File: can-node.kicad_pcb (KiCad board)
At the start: 2 copper layers, 50 x 60 mm, 109 parts, among them P1 Debug, P2 CONN_01X04, Q1 DMP6023LSS, Q10 BSS138, Q11 BSS84P, Q12 BSS84P, Q13 BSS84P, Q14 BSS84P, Q15 BSS84P, Q2 SFH3711, Q3 BSS138, Q4 BSS138, Q5 BSS138, Q6 BSS138, Q7 BSS138, Q8 BSS138, Q9 BSS138, SW1 SW_PUSH, SW2 SW_PUSH, SW3 SW_PUSH, U1 LMR16006, U2 SN74LVC1G08, U3 STM32F072RB, U4 HDC1080, U5 TCAN334, X1 32.768KHz 12.5pF

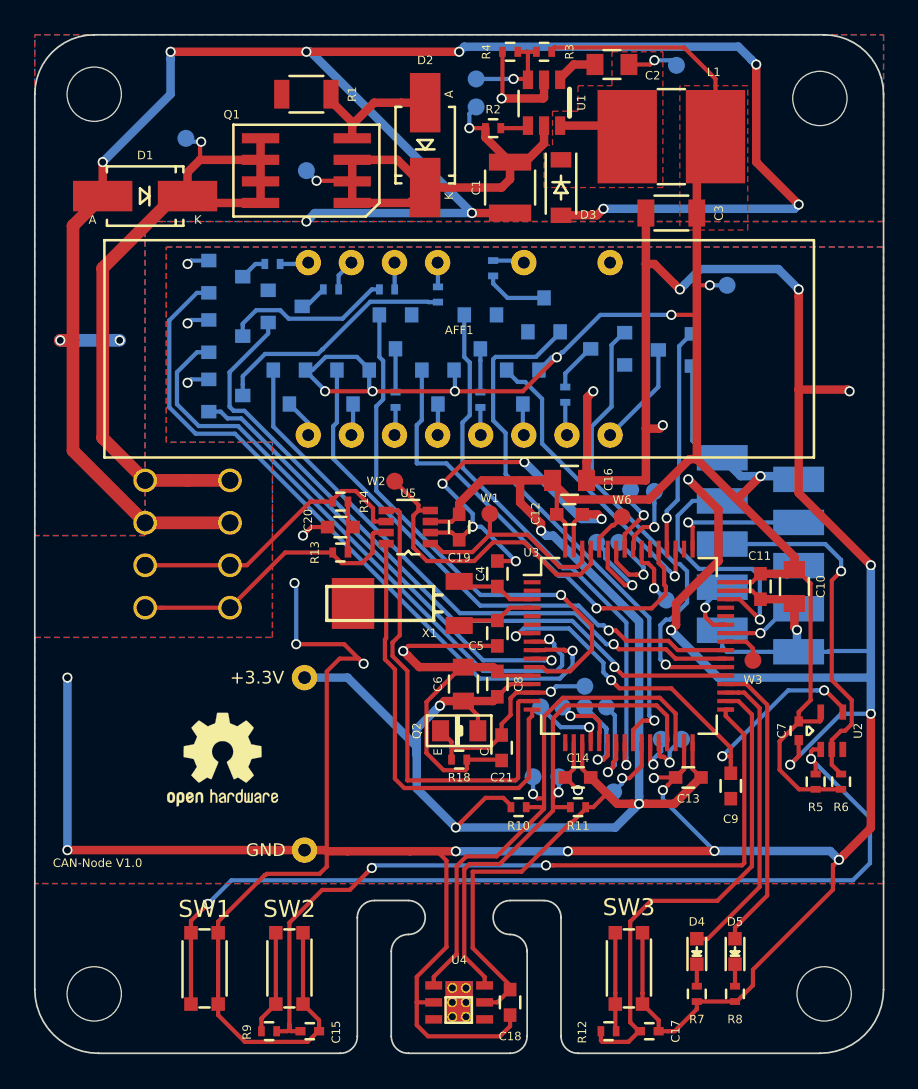
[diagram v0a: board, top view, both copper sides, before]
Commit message: Add buffer capacitor for RTC.
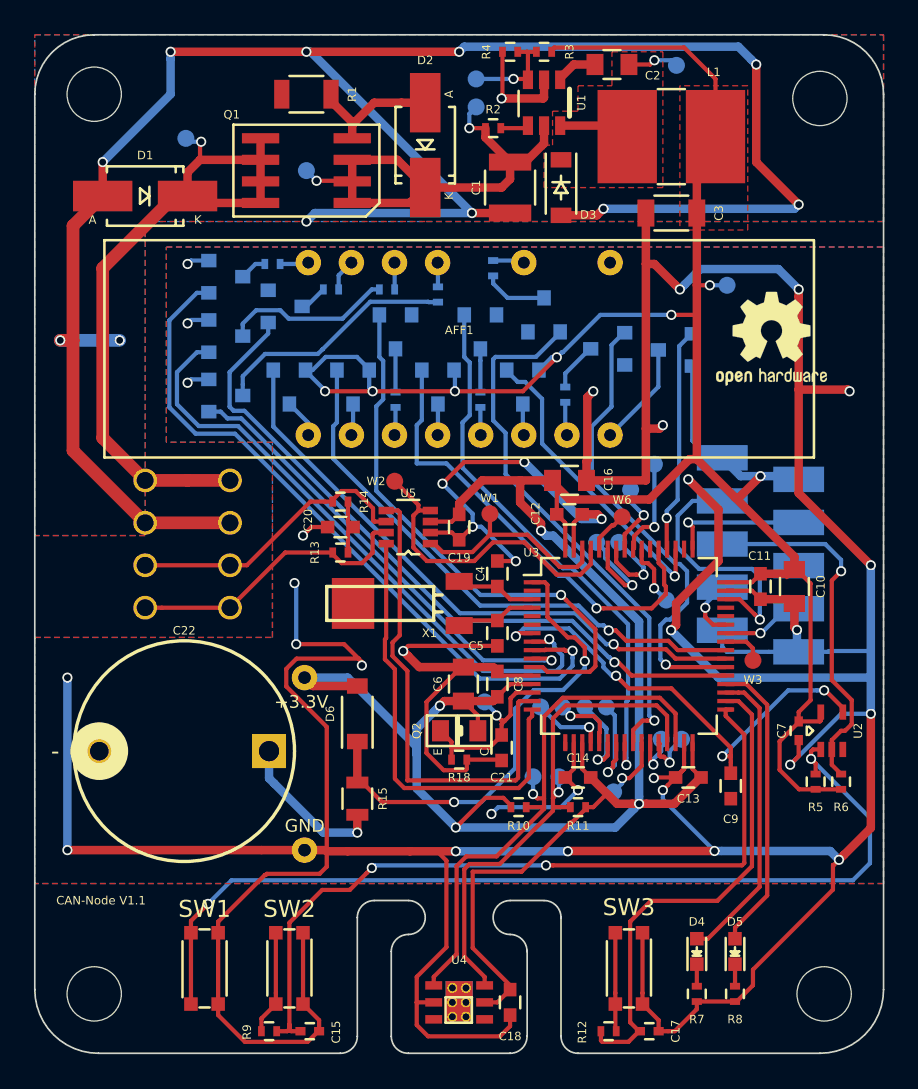
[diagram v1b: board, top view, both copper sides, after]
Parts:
- added C22: 0.1F, can-node:C_Radial_D13_L7_P10, F.Cu at (133.8, 107.2)
- added D6: 0.3V, Diodes_SMD:SOD-123, F.Cu at (139.0, 105.0)
- added R15: 100, Resistors_SMD:R_0805, F.Cu at (139.0, 110.0)
- R12, R9: value 220 -> 3.3k
- moved REF*** 40.7 mm to (163.4, 82.9)
- moved W18 5.97 mm to (146.5, 104.3)
- moved W35 1.60 mm to (156.5, 90.3)
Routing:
- net VBAT: track 0.00 -> 28.6 mm, vias 0 -> 2
- net GND: track 472.2 -> 481.4 mm, vias 45 -> 46
- net Net-(C22-Pad1): track 0.00 -> 9.18 mm, vias 0 -> 1
- net +3.3VADC: track 236.3 -> 239.7 mm
- net /Microcontroller/PB4: track 4.30 -> 5.90 mm
- net /Microcontroller/ADC_IN0: track 12.3 -> 10.8 mm
- net PC3: track 32.2 -> 33.1 mm
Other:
- board text added: "CAN-Node V1.1"
- board text removed: "CAN-Node V1.0"

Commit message: Make the board more hand solder friendly.
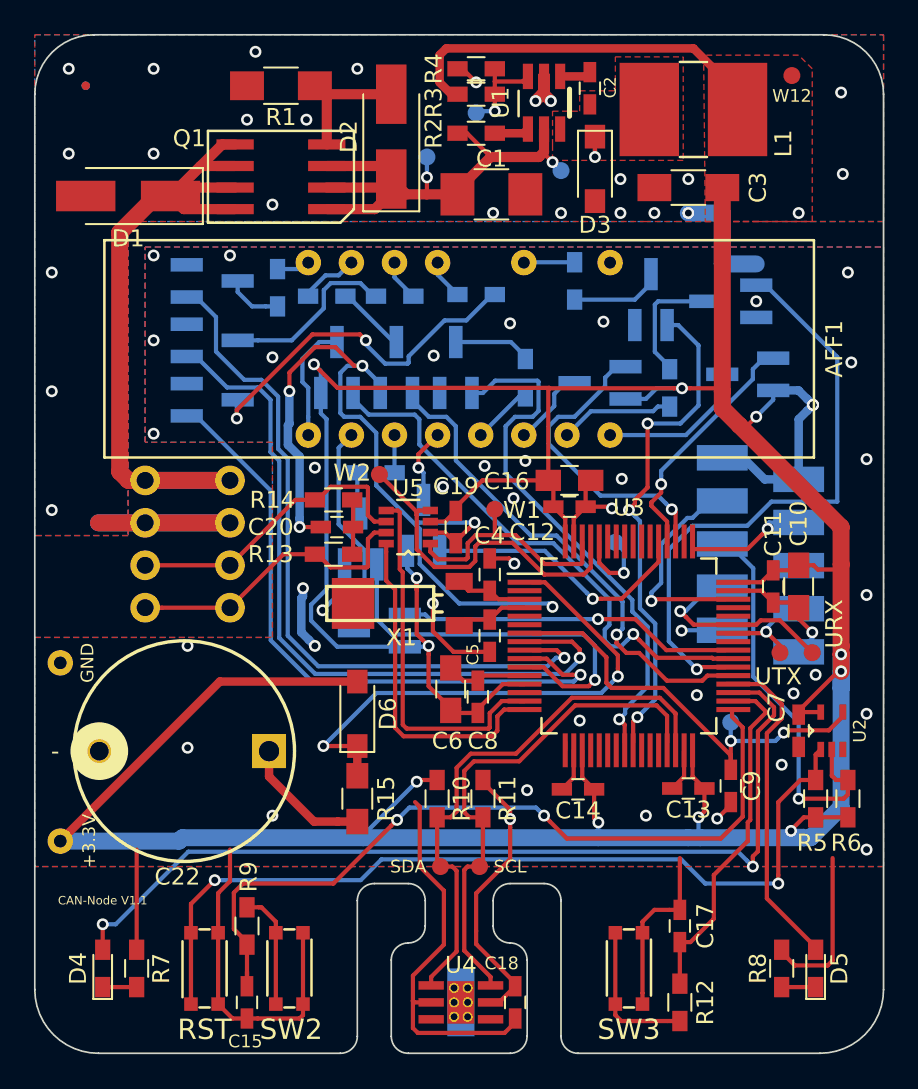
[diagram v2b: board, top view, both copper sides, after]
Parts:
- removed C21: 100n, Capacitors_SMD:C_0603
- removed Q2: SFH3711, can-node:SFH3711
- removed R18: 4.7k, Resistors_SMD:R_0402
- removed the REF** at (166.5, 121.5)
- removed the REF** at (166.2, 68.8)
- removed the REF** at (123.5, 68.5)
- removed the REF** at (123.5, 121.5)
- removed the REF*** at (163.4, 82.9)
- removed W13: PA5, can-node:Measurement_Point_tiny
- removed W14: PA4, can-node:Measurement_Point_tiny
- removed W18: LSENS, can-node:Measurement_Point_tiny
- removed W30: PB2, can-node:Measurement_Point_tiny
- removed W31: PB1, can-node:Measurement_Point_tiny
- removed W32: PB0, can-node:Measurement_Point_tiny
- removed W33, W34, W35, W36, W37: PB, can-node:Measurement_Point_tiny
- removed W4: PA7, can-node:Measurement_Point_tiny
- removed W5: PA6, can-node:Measurement_Point_tiny
- removed W7: VINA, can-node:Measurement_Point_tiny
- added REF**: Fiducial_0.5mm_Dia_1mm_Outer, Fiducials:Fiducial_0.5mm_Dia_1mm_Outer, F.Cu at (123.0, 68.0)
- added REF**: Fiducial_0.5mm_Dia_1mm_Outer, Fiducials:Fiducial_0.5mm_Dia_1mm_Outer, B.Cu at (123.0, 68.0)
- added REF***: OSHW-Logo_7.5x8mm_SilkScreen, Symbols:OSHW-Logo_7.5x8mm_SilkScreen, B.Cu at (160.5, 118.2)
- added URX: UART_RX, can-node:Measurement_Point_tiny, F.Cu at (165.8, 101.4)
- added UTX: UART_TX, can-node:Measurement_Point_tiny, F.Cu at (163.9, 101.4)
- C1: footprint Capacitors_SMD:C_1210 -> Capacitors_SMD:C_1210_HandSoldering
- C10, C16, C6: footprint Capacitors_SMD:C_0805 -> Capacitors_SMD:C_0805_HandSoldering
- C11, C12, C13, C14, C18, C19, C20, C4, C5, C8, C9: footprint Capacitors_SMD:C_0603 -> Capacitors_SMD:C_0603_HandSoldering
- C15, C17, C7: footprint Capacitors_SMD:C_0402 -> Capacitors_SMD:C_0603_HandSoldering
- C2: footprint Capacitors_SMD:C_0805 -> Capacitors_SMD:C_0603_HandSoldering
- C3: footprint Capacitors_SMD:C_1206 -> Capacitors_SMD:C_1206_HandSoldering
- D1, D2: footprint Diodes_SMD:SMA_Handsoldering -> Diodes_SMD:D_SMA_Handsoldering
- D3, D6: footprint Diodes_SMD:SOD-123 -> can-node:D_SOD-123_HandSoldering
- D4, D5: footprint LEDs:LED_0603 -> LEDs:LED_0603_HandSoldering
- L1: footprint CAN_Node:SDE0604A_HandSoldering -> can-node:SDE0604A_HandSoldering
- P1: footprint CAN_Node:micromatch_smd_2x05 -> can-node:micromatch_smd_2x05
- Q10, Q11, Q12, Q13, Q14, Q15, Q3, Q4, Q5, Q6, Q7, Q8, Q9: footprint TO_SOT_Packages_SMD:SOT-23 -> TO_SOT_Packages_SMD:SOT-23_Handsoldering
- R1: footprint Resistors_SMD:R_1206 -> Resistors_SMD:R_1206_HandSoldering
- R10, R11, R12, R13, R14, R2, R25, R26, R27, R28, R3, R33, R34, R35, R36, R4, R5, R6, R7, R8, R9: footprint Resistors_SMD:R_0402 -> Resistors_SMD:R_0603_HandSoldering
- R15: footprint Resistors_SMD:R_0805 -> Resistors_SMD:R_0805_HandSoldering
- SCL: renamed from W17; moved to F.Cu
- SDA: renamed from W16; moved to F.Cu
- SW2, SW3: footprint CAN_Node:KMR2 -> can-node:KMR2
- U1: footprint can-node:TI-DDC -> can-node:TI-DDC_HandSoldering
- U2: footprint CAN_Node:TI-DCK -> can-node:TI-DCK
- U3: footprint Housings_QFP:LQFP-64_10x10mm_Pitch0.5mm -> can-node:QFP-64_10x10_Pitch0.5mm_HandSoldering
- U4: footprint CAN_Node:HDC1080 -> can-node:HDC1080_HandSoldering
- U5: footprint CAN_Node:TI-DCN -> can-node:TI-DCN
- W12: moved to F.Cu
- W15: value TEST_1P -> 3.3V
- W19: value TEST_1P -> GND
- W3: value PA8 -> ~RST; moved to B.Cu
- W6: moved to B.Cu
- moved D4 35.0 mm to (124.0, 120.0)
- moved R7 33.0 mm to (126.0, 120.0), turned to 270 degrees
- moved W19 18.1 mm to (121.5, 102.0)
- moved W15 17.3 mm to (121.5, 112.5)
- moved Q12 14.4 mm to (140.3, 100.1), turned to 180 degrees
- moved W12 12.9 mm to (164.6, 67.4)
- moved Q6 12.4 mm to (139.2, 94.7), turned to 90 degrees
- moved Q15 8.19 mm to (142.9, 93.9), turned to 90 degrees
- moved Q10 7.77 mm to (161.0, 80.7)
- moved SDA 7.60 mm to (143.9, 114.0)
- moved Q9 7.47 mm to (141.3, 84.6), turned to 90 degrees
- moved W8 7.14 mm to (143.1, 72.2), turned to 0 degrees
- moved SCL 7.06 mm to (146.2, 114.0)
- moved C17 6.46 mm to (158.0, 117.5), turned to 90 degrees
- moved W11 6.38 mm to (153.0, 71.0), turned to 0 degrees
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- renumbered SW1 to RST
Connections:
- U3 pad 14: /Microcontroller/ADC_IN0 -> Net-(U3-Pad14)
- U3 pad 26: /Microcontroller/PB0 -> Net-(U3-Pad26)
- U3 pad 27: /Microcontroller/PB1 -> Net-(U3-Pad27)
- U3 pad 28: /Microcontroller/PB2 -> Net-(U3-Pad28)
- U3 pad 55: /Microcontroller/PB3 -> Net-(U3-Pad55)
- U3 pad 56: /Microcontroller/PB4 -> Net-(U3-Pad56)
- U3 pad 57: /Microcontroller/PB5 -> Net-(U3-Pad57)
- U3 pad 58: /Microcontroller/PB6 -> Net-(U3-Pad58)
- U3 pad 59: /Microcontroller/PB7 -> Net-(U3-Pad59)
- W3 pad 1: Net-(U3-Pad41) -> Net-(C9-Pad1)
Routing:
- net GND: track 481.4 -> 185.2 mm, vias 46 -> 69
- net +3.3VADC: track 239.7 -> 287.4 mm, vias 11 -> 15
- net Net-(D4-Pad2): track 17.9 -> 55.0 mm, vias 0 -> 2
- net PC9: track 33.1 -> 19.8 mm
- net PC6: track 41.7 -> 29.0 mm
- net PC12: track 27.1 -> 15.7 mm
- net Net-(AFF1-Pad2): track 1.87 -> 12.7 mm
- net PC2: track 27.4 -> 38.3 mm
- net /Microcontroller/ADC_IN0: track 10.8 -> 0.00 mm, vias 1 -> 0
- net PC3: track 33.1 -> 23.1 mm
- net PC7: track 27.4 -> 35.6 mm
- net /Microcontroller/UART1_RX: track 3.56 -> 11.6 mm
- net Net-(C17-Pad1): track 29.2 -> 21.1 mm
- net Net-(U3-Pad22): track 7.25 -> 0.00 mm, vias 1 -> 0
- net Net-(Q5-Pad3): track 14.5 -> 21.4 mm, vias 0 -> 2
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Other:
- outline, holes or cut-outs redrawn
- net class Default: via_dia 0.6 -> 0.7
- net class Power: via_dia 0.6 -> 0.7
- rule via_min_drill: 0.3 -> 0.4
- rule via_min_size: 0.4 -> 0.7
- board text added: "+"
- board text added: "-"
- board text added: "2018-01-05"
- board text added: "CAN Node Rev 1.1"
- board text added: "CH"
- board text added: "CL"
- board text added: "designed with KiCad"
- board text removed: "3.3V"
- board text removed: "CANH"
- board text removed: "CANL"
- board text removed: "SWCLK"
- board text removed: "SWDIO"
- board text removed: "U_TX"
- board text removed: "VIN+/24V DC"
- board text removed: "VIN-/0V"
- board text removed: "designed with KiCAD"
- board text removed: "© 2017 Josef Raschen"

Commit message: Add mounting holes.
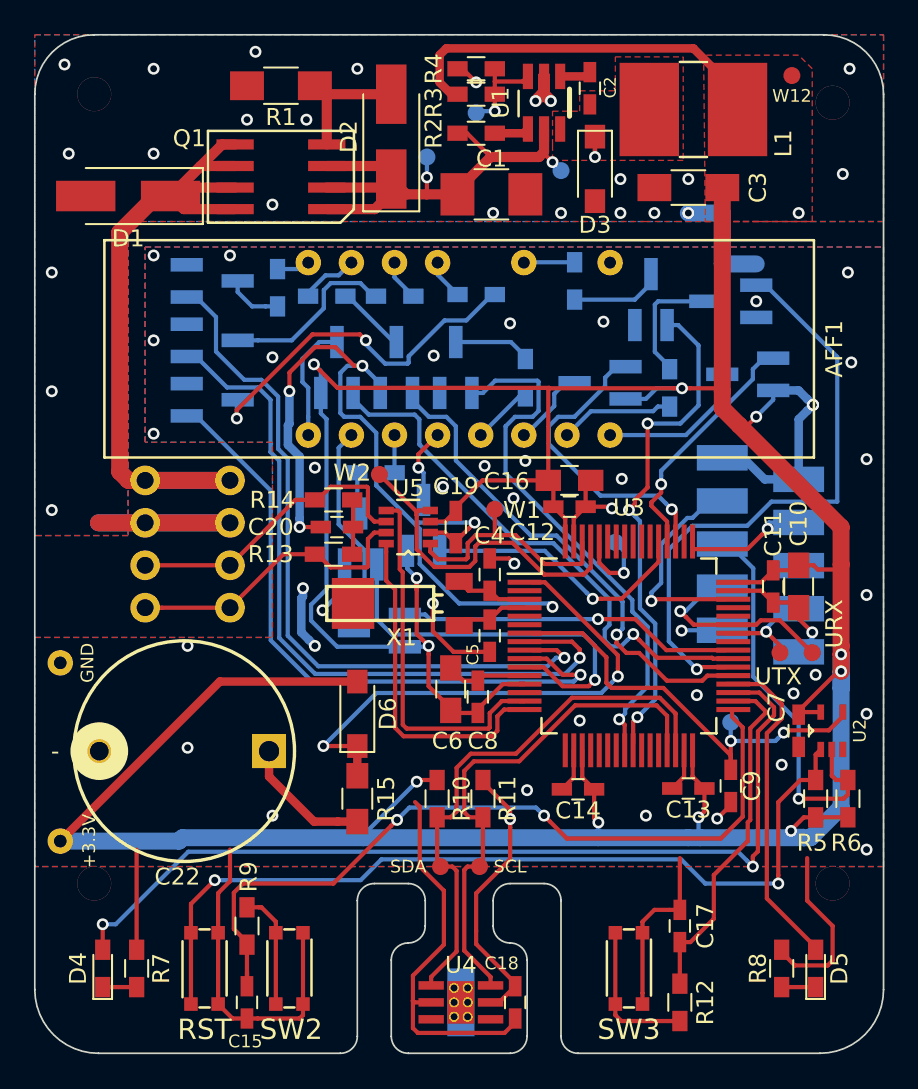
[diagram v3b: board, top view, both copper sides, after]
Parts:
- removed the REF** at (123.0, 68.0) (x2)
- added REF**: NPTH_2mm, can-node:NPTH_2mm, F.Cu at (167.0, 115.0)
- added REF**: NPTH_2mm, can-node:NPTH_2mm, F.Cu at (123.5, 115.0)
- added REF**: NPTH_2mm, can-node:NPTH_2mm, F.Cu at (167.0, 69.0)
- added REF**: NPTH_2mm, can-node:NPTH_2mm, F.Cu at (123.5, 68.5)
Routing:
- net GND: track 185.2 -> 185.8 mm
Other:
- board text removed: "CAN-Node V1.1"
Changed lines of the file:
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@@
   (general
     (thickness 1.6)
-    (drawings 75)
-    (tracks 993)
+    (drawings 74)
+    (tracks 995)
     (zones 0)
-    (modules 95)
+    (modules 97)
     (nets 98)
   )
@@
   )
   (setup
-    (last_trace_width 1)
+    (last_trace_width 0.25)
     (user_trace_width 0.2)
     (user_trace_width 0.5)
@@
     (mod_text_size 1 1)
     (mod_text_width 0.2)
-    (pad_size 1.5 1.5)
-    (pad_drill 0.6)
+    (pad_size 2 2)
+    (pad_drill 2)
     (pad_to_mask_clearance 0)
     (aux_axis_origin 0 0)
@@
     (add_net VIN+)
   )
+  (module can-node:NPTH_2mm (layer F.Cu)
+    (at 167 115)
+    (fp_text reference REF** (at 0 0.5) (layer F.SilkS) hide
+      (effects (font (size 1 1) (thickness 0.15)))
+    )
+    (fp_text value NPTH_2mm (at 0 -0.5) (layer F.Fab) hide
+      (effects (font (size 1 1) (thickness 0.15)))
+    )
+    (pad "" thru_hole circle (at 0 0) (size 2 2) (drill 2) (layers *.Cu *.Mask))
+  )
+  (module can-node:NPTH_2mm (layer F.Cu)
+    (at 123.5 115)
+    (fp_text reference REF** (at 0 0.5) (layer F.SilkS) hide
+      (effects (font (size 1 1) (thickness 0.15)))
+    )
+    (fp_text value NPTH_2mm (at 0 -0.5) (layer F.Fab) hide
+      (effects (font (size 1 1) (thickness 0.15)))
+    )
+    (pad "" thru_hole circle (at 0 0) (size 2 2) (drill 2) (layers *.Cu *.Mask))
+  )
+  (module can-node:NPTH_2mm (layer F.Cu)
+    (at 167 69)
+    (fp_text reference REF** (at 0 0.5) (layer F.SilkS) hide
+      (effects (font (size 1 1) (thickness 0.15)))
+    )
+    (fp_text value NPTH_2mm (at 0 -0.5) (layer F.Fab) hide
+      (effects (font (size 1 1) (thickness 0.15)))
+    )
+    (pad "" thru_hole circle (at 0 0) (size 2 2) (drill 2) (layers *.Cu *.Mask))
+  )
+  (module can-node:NPTH_2mm (layer F.Cu)
+    (at 123.5 68.5)
+    (fp_text reference REF** (at 0 0.5) (layer F.SilkS) hide
+      (effects (font (size 1 1) (thickness 0.15)))
+    )
+    (fp_text value NPTH_2mm (at 0 -0.5) (layer F.Fab) hide
+      (effects (font (size 1 1) (thickness 0.15)))
+    )
+    (pad "" thru_hole circle (at 0 0) (size 2 2) (drill 2) (layers *.Cu *.Mask))
+  )
   (module can-node:HDC1080_HandSoldering (layer F.Cu)
     (at 145.1 122 270)
@@
       (net 5 +3.3VADC))
   )
-  (module Fiducials:Fiducial_0.5mm_Dia_1mm_Outer (layer F.Cu)
-    (at 123 68)
-    (descr "Circular Fiducial, 0.5mm bare copper top; 1mm keepout (Level C)")
-    (tags marker)
-    (attr virtual)
-    (fp_text reference REF** (at 0 -1.5) (layer F.SilkS) hide
-      (effects (font (size 1 1) (thickness 0.15)))
-    )
-    (fp_text value Fiducial_0.5mm_Dia_1mm_Outer (at 0 1.5) (layer F.Fab)
-      (effects (font (size 1 1) (thickness 0.15)))
-    )
-    (fp_circle (center 0 0) (end 0.5 0) (layer F.Fab) (width 0.1))
-    (fp_text user %R (at 0 0) (layer F.Fab)
-      (effects (font (size 0.2 0.2) (thickness 0.04)))
-    )
-    (fp_circle (center 0 0) (end 0.75 0) (layer F.CrtYd) (width 0.05))
-    (pad ~ smd circle (at 0 0) (size 0.5 0.5) (layers F.Cu F.Mask)
-      (solder_mask_margin 0.25) (clearance 0.25))
-  )
-  (module Fiducials:Fiducial_0.5mm_Dia_1mm_Outer (layer B.Cu)
-    (at 123 68)
-    (descr "Circular Fiducial, 0.5mm bare copper top; 1mm keepout (Level C)")
-    (tags marker)
-    (attr virtual)
-    (fp_text reference REF** (at 0 1.5) (layer B.SilkS) hide
-      (effects (font (size 1 1) (thickness 0.15)) (justify mirror))
-    )
-    (fp_text value Fiducial_0.5mm_Dia_1mm_Outer (at 0 -1.5) (layer B.Fab)
-      (effects (font (size 1 1) (thickness 0.15)) (justify mirror))
-    )
-    (fp_circle (center 0 0) (end 0.5 0) (layer B.Fab) (width 0.1))
-    (fp_text user %R (at 0 0) (layer B.Fab)
-      (effects (font (size 0.2 0.2) (thickness 0.04)) (justify mirror))
-    )
-    (fp_circle (center 0 0) (end 0.75 0) (layer B.CrtYd) (width 0.05))
-    (pad ~ smd circle (at 0 0) (size 0.5 0.5) (layers B.Cu B.Mask)
-      (solder_mask_margin 0.25) (clearance 0.25))
-  )
   (module Symbols:OSHW-Logo_7.5x8mm_SilkScreen (layer B.Cu)
     (at 160.5 118.2 180)
@@
   (gr_arc (start 142 117.5) (end 143 117.5) (angle 90) (layer Edge.Cuts) (width 0.1))
   (gr_arc (start 148 117.5) (end 148 118.5) (angle 90) (layer Edge.Cuts) (width 0.1))
-  (gr_text "CAN-Node V1.1" (at 124 116) (layer F.SilkS)
-    (effects (font (size 0.5 0.5) (thickness 0.125)))
-  )
   (gr_text +3.3V (at 123.2 112.5 90) (layer F.SilkS)
     (effects (font (size 0.75 0.75) (thickness 0.15)))
@@
   (segment (start 144.9 67) (end 145.2 67) (width 0.25) (layer F.Cu) (net 2))
   (segment (start 145.2 67) (end 146 67.8) (width 0.25) (layer F.Cu) (net 2))
-  (via (at 122 67) (size 0.7) (drill 0.4) (layers F.Cu B.Cu) (net 2))
+  (via (at 121.75 66.75) (size 0.7) (drill 0.4) (layers F.Cu B.Cu) (net 2))
   (via (at 127 67) (size 0.7) (drill 0.4) (layers F.Cu B.Cu) (net 2))
   (via (at 122 72) (size 0.7) (drill 0.4) (layers F.Cu B.Cu) (net 2))
   (via (at 127 72) (size 0.7) (drill 0.4) (layers F.Cu B.Cu) (net 2))
-  (via (at 167.5 68.4) (size 0.7) (drill 0.4) (layers F.Cu B.Cu) (net 2))
+  (via (at 168 67) (size 0.7) (drill 0.4) (layers F.Cu B.Cu) (net 2))
   (via (at 167.6 73.2) (size 0.7) (drill 0.4) (layers F.Cu B.Cu) (net 2))
   (via (at 167.9 79) (size 0.7) (drill 0.4) (layers F.Cu B.Cu) (net 2))
@@
   (segment (start 164.775001 119.825001) (end 166.710001 119.825001) (width 0.25) (layer F.Cu) (net 2))
   (segment (start 164 119.05) (end 164.775001 119.825001) (width 0.25) (layer F.Cu) (net 2))
-  (segment (start 167 119.535002) (end 167 113.5) (width 0.25) (layer F.Cu) (net 2))
   (segment (start 130.8 122.1) (end 130.8 117.9) (width 0.25) (layer F.Cu) (net 2))
   (segment (start 126 118.9) (end 126 113) (width 0.25) (layer F.Cu) (net 2))
@@
   (via (at 134 111) (size 0.7) (drill 0.4) (layers F.Cu B.Cu) (net 2))
   (via (at 129 101) (size 0.7) (drill 0.4) (layers F.Cu B.Cu) (net 2))
+  (segment (start 167 117.5) (end 165.5 116) (width 0.25) (layer F.Cu) (net 2))
+  (segment (start 167 119.535002) (end 167 117.5) (width 0.25) (layer F.Cu) (net 2))
+  (segment (start 165.5 116) (end 165.5 113.5) (width 0.25) (layer F.Cu) (net 2))
   (via (at 153 72.2) (size 0.7) (drill 0.4) (layers F.Cu B.Cu) (net 3))
   (segment (start 153 71) (end 153 72.2) (width 0.25) (layer B.Cu) (net 3))
